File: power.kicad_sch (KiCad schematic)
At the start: 61 parts, among them T1 net-tie, U1 LMR54410, U11 RT9080-33GJ5, U5 MIC5504, U6 INA219AID

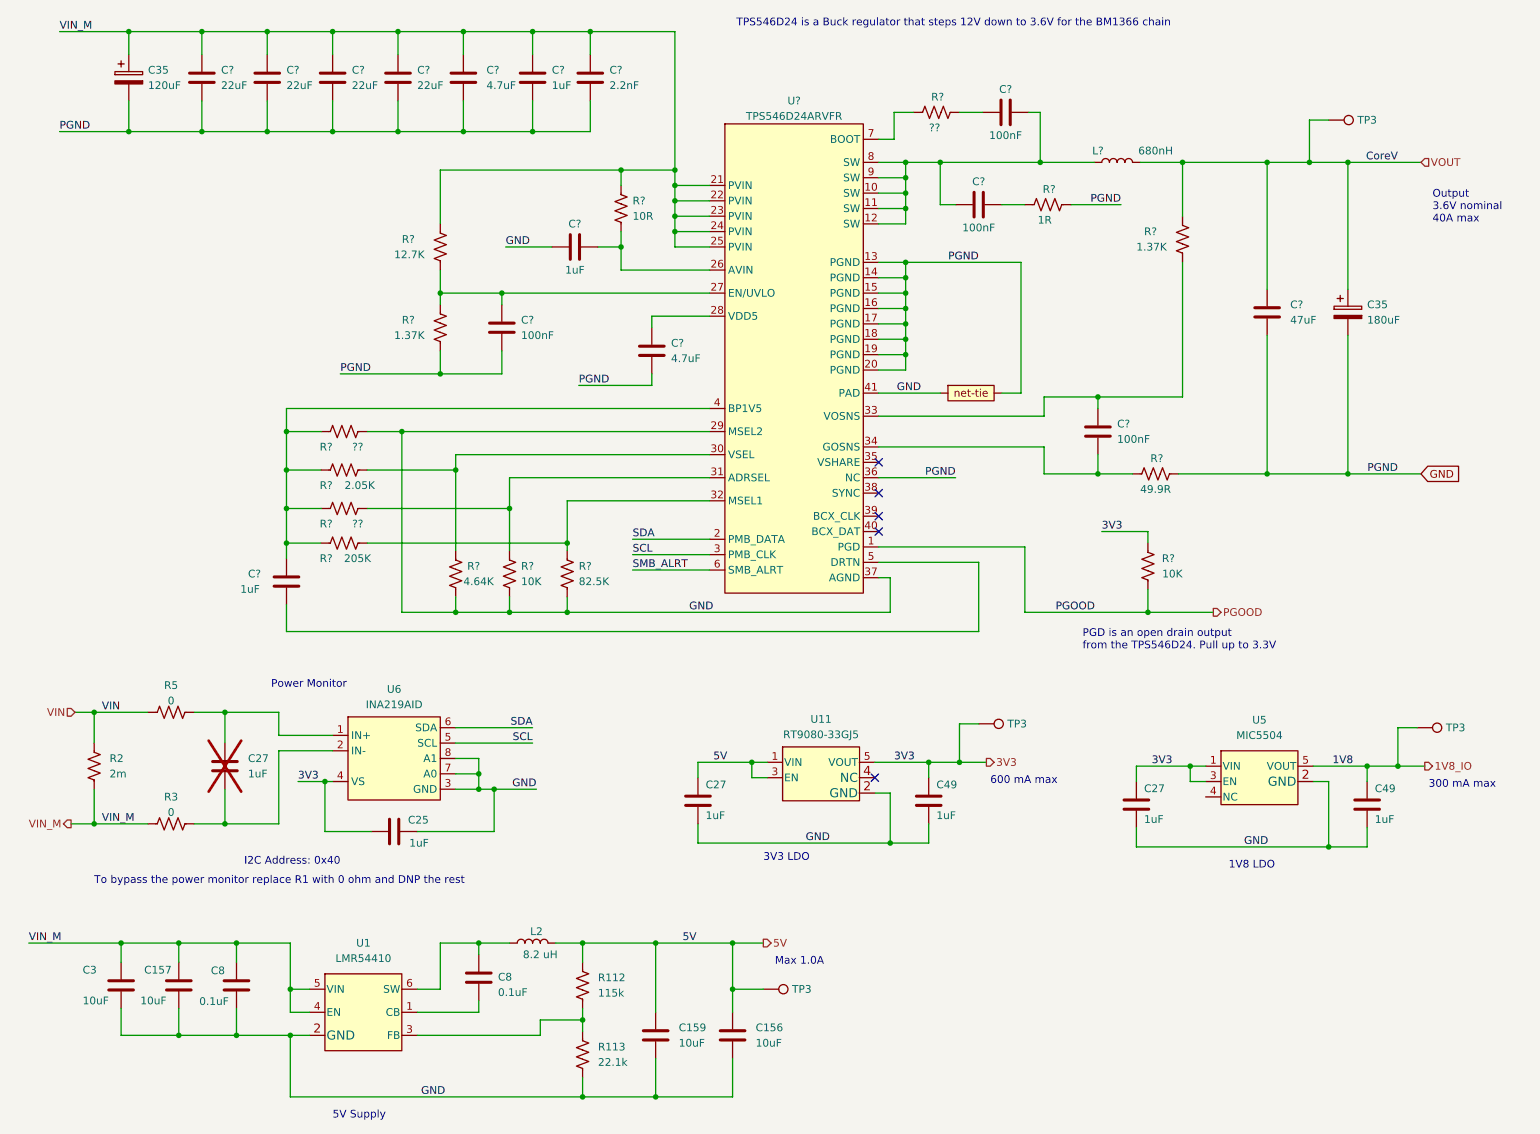
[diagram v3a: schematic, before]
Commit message: remove INA219 power monitor
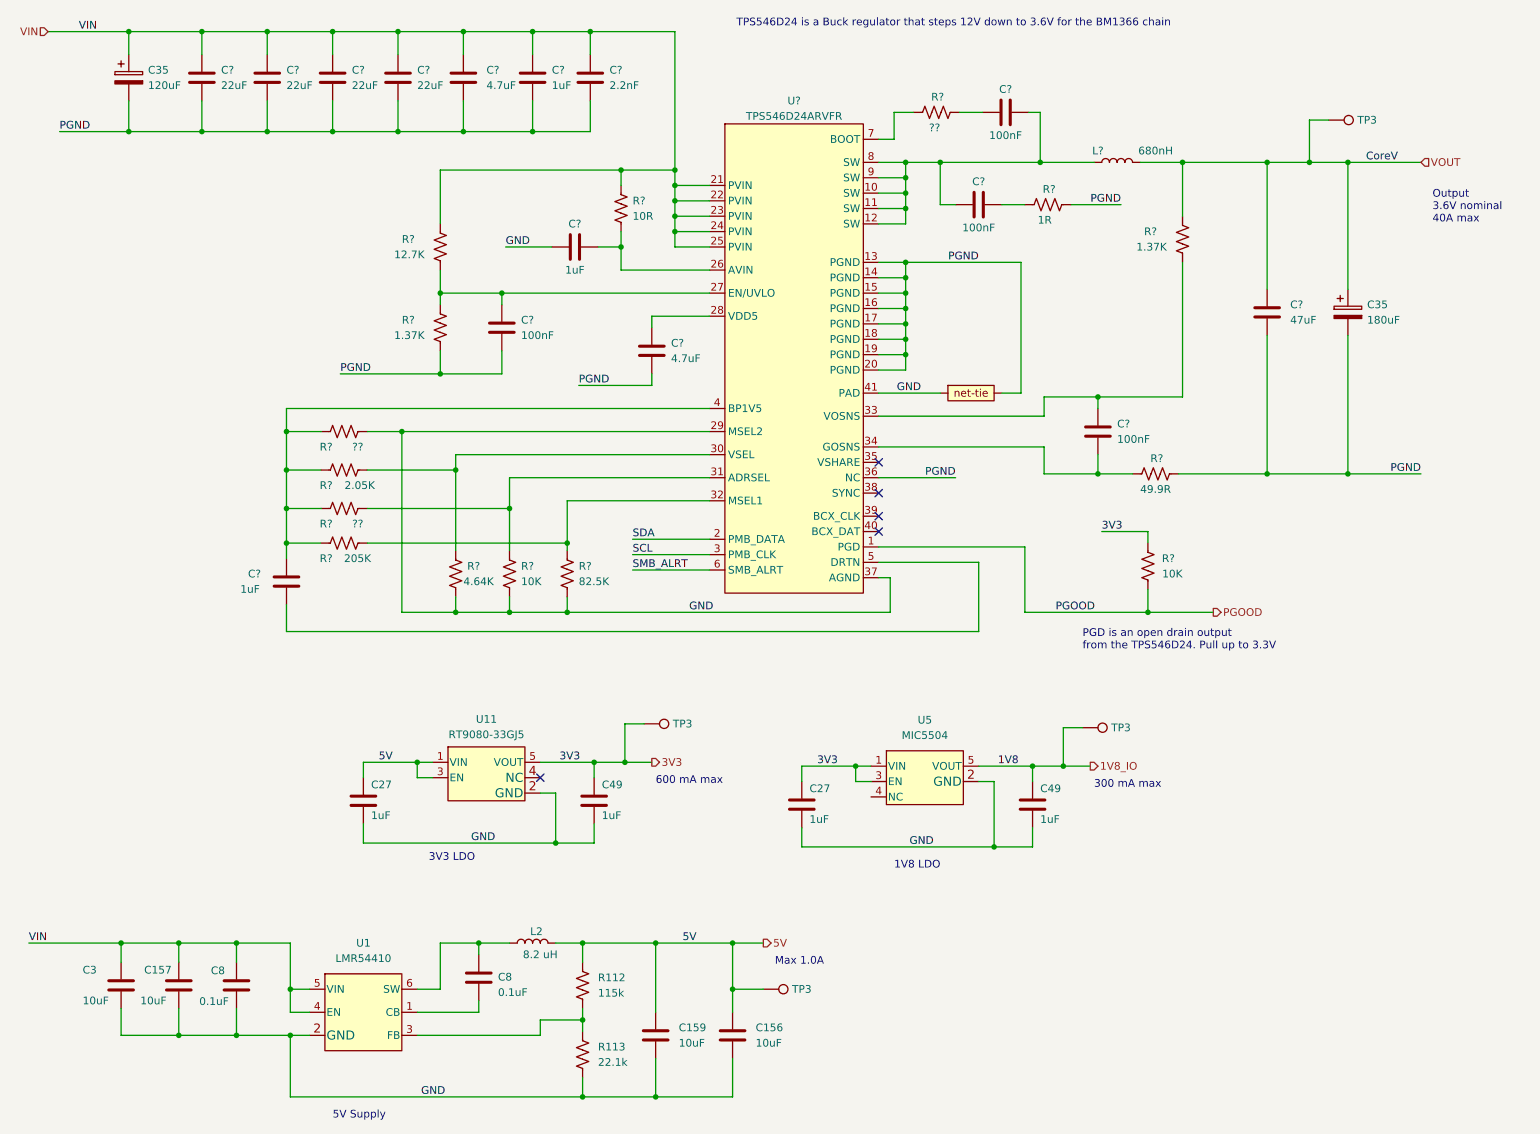
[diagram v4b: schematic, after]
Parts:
- removed C25, C27: 1uF, Capacitor_SMD:C_0402_1005Metric, symbol Device:C
- removed R2: 2m, Resistor_SMD:R_1206_3216Metric, symbol Device:R_US
- removed R3, R5: 0, Resistor_SMD:R_0402_1005Metric, symbol Device:R_US
- removed U6: INA219AID, Package_TO_SOT_SMD:SOT-23-8, symbol bitaxe:INA219AIDCNR
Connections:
- net VIN_M is gone; now on net VIN: C157.1, C3.1, C35.1, C8.2, C?.1, C?.1, C?.1, C?.1, C?.1, C?.1, C?.1, R?.1, R?.1, U1.4 (EN), U1.5 (VIN), U?.21 (PVIN), U?.22 (PVIN), U?.23 (PVIN), U?.24 (PVIN), U?.25 (PVIN)
- net GND: no longer C35.2, C35.2, C?.2, C?.2, C?.2, C?.2, C?.2, C?.2, C?.2, C?.2, C?.2, C?.2, R?.2, R?.2, R?.2, U?.13 (PGND), U?.14 (PGND), U?.15 (PGND), U?.16 (PGND), U?.17 (PGND), U?.18 (PGND), U?.19 (PGND), U?.20 (PGND), U?.36 (NC)
- new net PGND: C35.2, C35.2, C?.2, C?.2, C?.2, C?.2, C?.2, C?.2, C?.2, C?.2, C?.2, C?.2, R?.2, R?.2, R?.2, T1., U?.13 (PGND), U?.14 (PGND), U?.15 (PGND), U?.16 (PGND), U?.17 (PGND), U?.18 (PGND), U?.19 (PGND), U?.20 (PGND), U?.36 (NC)
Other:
- note removed: "I2C Address: 0x40"
- note removed: "Power Monitor"
- note removed: "To bypass the power monitor replace R1 with 0 ohm and DNP the rest"
- moved on the sheet: C27, C49, TP3, U11, U5

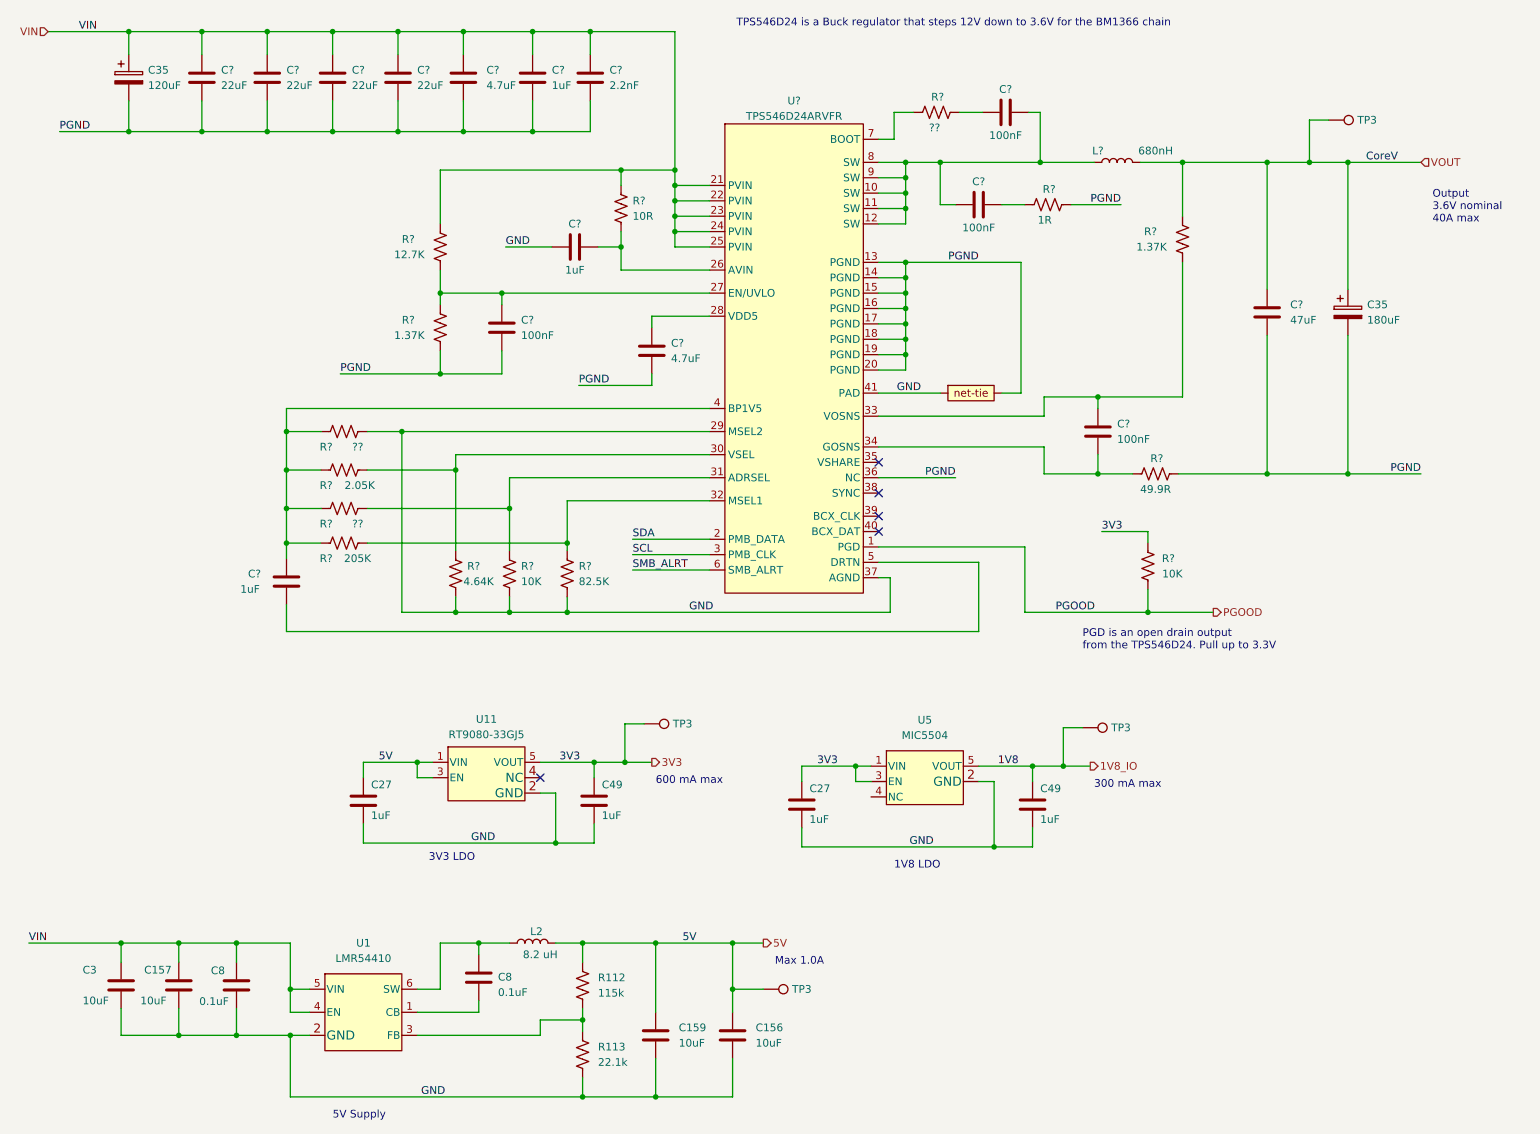
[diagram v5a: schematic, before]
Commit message: start parts placement for TPS546D24 regulator
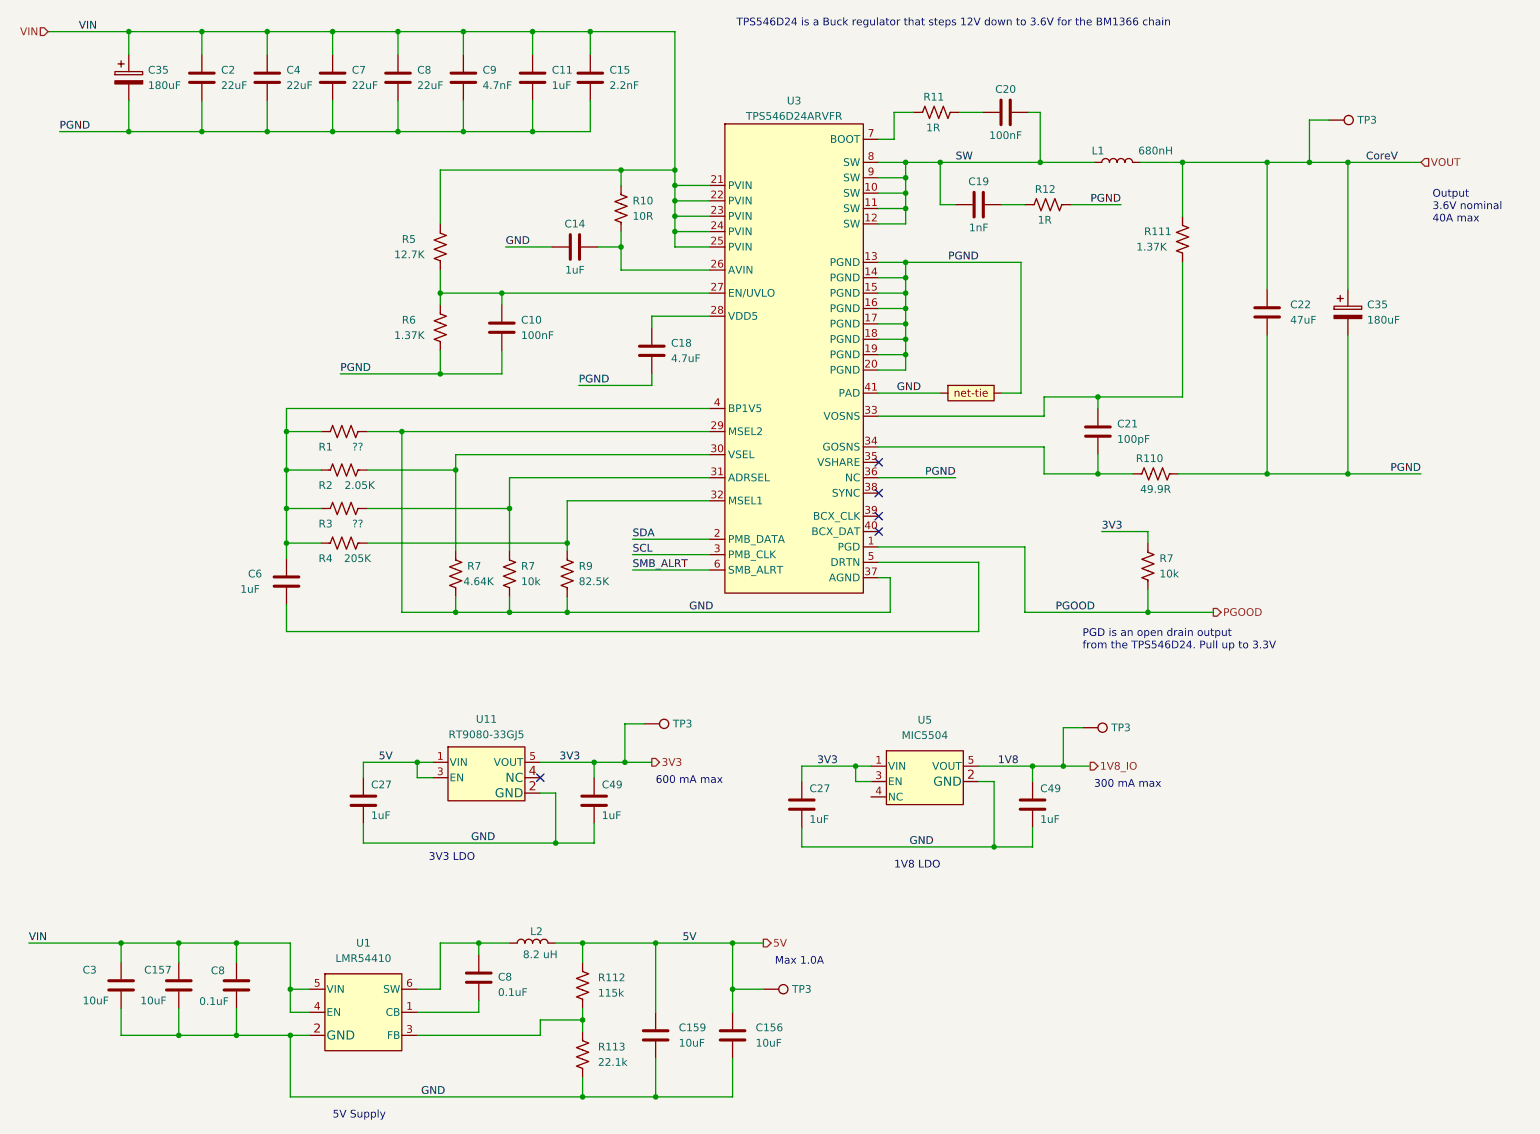
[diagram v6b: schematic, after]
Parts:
- removed C? (x3): 22uF, Capacitor_SMD:C_1210_3225Metric, symbol Device:C
- removed R? (x2): 10K, Resistor_SMD:R_0402_1005Metric, symbol Device:R_US
- added C4, C7, C8: 22uF, Capacitor_SMD:C_1210_3225Metric, symbol Device:C
- added R7 (x2): 10k, Resistor_SMD:R_0402_1005Metric, symbol Device:R_US
- C10: renamed from C?; footprint Capacitor_SMD:C_1210_3225Metric -> Capacitor_SMD:C_0402_1005Metric; DK 1276-3363-1-ND -> 490-6321-1-ND; PARTNO CL32A106KBJNNNE -> GRM155R71A104KA01D
- C11: renamed from C?; footprint Capacitor_SMD:C_1210_3225Metric -> Capacitor_SMD:C_0805_2012Metric; DK 1276-3363-1-ND -> 587-1291-1-ND; PARTNO CL32A106KBJNNNE -> TMK212BJ105KG-T
- C14: renamed from C?; footprint Capacitor_SMD:C_0402_1005Metric -> Capacitor_SMD:C_0805_2012Metric; DK 13-CC0402JPNPO9BN121CT-ND -> 587-1291-1-ND; PARTNO CC0402JPNPO9BN121 -> TMK212BJ105KG-T
- C15: renamed from C?; footprint Capacitor_SMD:C_1210_3225Metric -> Capacitor_SMD:C_0402_1005Metric; DK 1276-3363-1-ND -> 490-8257-1-ND; PARTNO CL32A106KBJNNNE -> GRM155R61H222KA01D
- C18: renamed from C?; footprint Capacitor_SMD:C_1210_3225Metric -> Capacitor_SMD:C_0402_1005Metric; DK 1276-3363-1-ND -> 490-14306-1-ND; PARTNO CL32A106KBJNNNE -> GRM155R61A475MEAAD
- C19: renamed from C?; value 100nF -> 1nF; footprint Capacitor_SMD:C_0402_1005Metric -> Capacitor_SMD:C_0805_2012Metric; DK 13-CC0402JPNPO9BN121CT-ND -> 311-1127-1-ND; PARTNO CC0402JPNPO9BN121 -> CC0805KRX7R9BB102
- C2: renamed from C?; DK 1276-1101-1-ND -> 490-3889-1-ND; PARTNO CL32A226KAJNNNE -> GRM32ER61E226KE15L
- C20: renamed from C?; footprint Capacitor_SMD:C_0402_1005Metric -> Capacitor_SMD:C_0805_2012Metric; DK 13-CC0402JPNPO9BN121CT-ND -> 478-KGM21NR71E104KTCT-ND; PARTNO CC0402JPNPO9BN121 -> KGM21NR71E104KT
- C21: renamed from C?; value 100nF -> 100pF; footprint Capacitor_SMD:C_1210_3225Metric -> Capacitor_SMD:C_0402_1005Metric; DK 1276-3363-1-ND -> 732-7431-1-ND; PARTNO CL32A106KBJNNNE -> 885012005013
- C22: renamed from C?; DK 1276-1101-1-ND -> 490-6539-1-ND; PARTNO CL32A226KAJNNNE -> GRM32ER61C476KE15L
- C35: footprint Capacitor_SMD:CP_Elec_6.3x7.7 -> Capacitor_SMD:CP_Elec_6.3x5.9; DK 732-8422-1-ND -> P16479CT-ND; PARTNO 865080345012 -> 16SVPF180M
- C35: value 120uF -> 180uF; footprint Capacitor_SMD:CP_Elec_6.3x7.7 -> Capacitor_SMD:CP_Elec_6.3x5.9; DK 732-8422-1-ND -> P16479CT-ND; PARTNO 865080345012 -> 16SVPF180M
- C6: renamed from C?; footprint Capacitor_SMD:C_1210_3225Metric -> Capacitor_SMD:C_0603_1608Metric; DK 1276-3363-1-ND -> 490-1550-1-ND; PARTNO CL32A106KBJNNNE -> GRM188R60J105KA01D
- C9: renamed from C?; value 4.7uF -> 4.7nF; footprint Capacitor_SMD:C_1210_3225Metric -> Capacitor_SMD:C_0402_1005Metric; DK 1276-1101-1-ND -> 490-1309-1-ND; PARTNO CL32A226KAJNNNE -> GRM155R71E472KA01D
- L1: renamed from L?; footprint bitaxe:744373580047 -> Inductor_SMD:L_Coilcraft_XAL1010-XXX; DK 732-7221-1-ND -> 2457-XAL1010-681MED-ND; Mouser (none) -> 994-XAL1010-681MED; PARTNO 744373580047 -> XAL1010-681MED
- R1, R3: renamed from R?; DK YAG2958CT-ND -> (none); PARTNO RC0402FR-0711K8L -> (none)
- R10: renamed from R?; DK YAG2958CT-ND -> 311-10.0LRCT-ND; PARTNO RC0402FR-0711K8L -> RC0402FR-0710RL
- R11: renamed from R?; value ?? -> 1R; DK YAG2958CT-ND -> (none); PARTNO RC0402FR-0711K8L -> (none)
- R110: renamed from R?; DK YAG2958CT-ND -> 311-49.9LRCT-ND; PARTNO RC0402FR-0711K8L -> RC0402FR-0749R9L
- R111, R6: renamed from R?; DK YAG2958CT-ND -> YAG3035CT-ND; PARTNO RC0402FR-0711K8L -> RC0402FR-071K37L
- R12: renamed from R?; footprint Resistor_SMD:R_0402_1005Metric -> Resistor_SMD:R_1206_3216Metric; DK YAG2958CT-ND -> CSR1206FT1R00CT-ND; PARTNO RC0402FR-0711K8L -> CSR1206FT1R00
- R2: renamed from R?; DK YAG2958CT-ND -> YAG3096CT-ND; PARTNO RC0402FR-0711K8L -> RC0402FR-072K05L
- R4: renamed from R?; DK YAG2958CT-ND -> YAG3050CT-ND; PARTNO RC0402FR-0711K8L -> RC0402FR-07205KL
- R5: renamed from R?; DK YAG2958CT-ND -> YAG2964CT-ND; PARTNO RC0402FR-0711K8L -> RC0402FR-0712K7L
- R7: renamed from R?; DK YAG2958CT-ND -> 311-4.64KLRCT-ND; PARTNO RC0402FR-0711K8L -> RC0402FR-074K64L
- R9: renamed from R?; DK YAG2958CT-ND -> 311-82.5KLRCT-ND; PARTNO RC0402FR-0711K8L -> RC0402FR-0782K5L
- U3: renamed from U?; footprint (none) -> bitaxe:LQFN40-CLIP
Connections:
- net 3V3: now also R7.2
- net GND: now also R7.1
- net PGND: now also C4.2, C7.2, C8.2
- net PGOOD: now also R7.1
- net VIN: now also C4.1, C7.1, C8.1
- net SW: now reaches C19.1, C20.2, L1.1, U3.10 (SW), U3.11 (SW), U3.12 (SW), U3.8 (SW), U3.9 (SW)
- net at R3.2, U3.31 (ADRSEL): now also R7.2

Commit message: parts placement for new regulator
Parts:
- C35: HEIGHT (none) -> 5.9mm
- L1: HEIGHT (none) -> 10mm
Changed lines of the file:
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@@
       (effects (font (size 1.27 1.27)) hide)
     )
-    (property "Datasheet" "https://industrial.panasonic.com/ww/products/pt/os-con/models/16SVPF180M" (at 235.585 66.675 0)
+    (property "Datasheet" "https://industrial.panasonic.com/cdbs/www-data/pdf/AAB8000/AAB8000C177.pdf" (at 235.585 66.675 0)
       (effects (font (size 1.27 1.27)) hide)
     )
@@
     )
     (property "PARTNO" "16SVPF180M" (at 235.585 66.675 0)
+      (effects (font (size 1.27 1.27)) hide)
+    )
+    (property "HEIGHT" "5.9mm" (at 235.585 66.675 0)
       (effects (font (size 1.27 1.27)) hide)
     )
@@
     )
     (property "Mouser" "994-XAL1010-681MED" (at 197.485 41.91 90)
+      (effects (font (size 1.27 1.27)) hide)
+    )
+    (property "HEIGHT" "10mm" (at 197.485 41.91 90)
       (effects (font (size 1.27 1.27)) hide)
     )
@@
       (effects (font (size 1.27 1.27)) hide)
     )
-    (property "Datasheet" "https://industrial.panasonic.com/ww/products/pt/os-con/models/16SVPF180M" (at 34.29 27.94 0)
+    (property "Datasheet" "https://industrial.panasonic.com/cdbs/www-data/pdf/AAB8000/AAB8000C177.pdf" (at 34.29 27.94 0)
       (effects (font (size 1.27 1.27)) hide)
     )
@@
       (effects (font (size 1.27 1.27)) hide)
     )
+    (property "HEIGHT" "5.9mm" (at 34.29 27.94 0)
+      (effects (font (size 1.27 1.27)) hide)
+    )
